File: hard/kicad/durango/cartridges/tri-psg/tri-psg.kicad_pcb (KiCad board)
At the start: 2 copper layers, 99.7 x 63.5 mm, 54 parts, among them J1 Durango_ROM, J2 CARTRIDGE, J20 PHONES, U1 74HC138, U10 SN76489A, U11 74HC574, U2 74HC08, U20 SN76489A, U21 74HC574, U22 SN76489A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

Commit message: cleanup and final triPSG opt
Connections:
- U2 pad 1: /LRDY -> /A4
- U2 pad 11: /A1·4 -> /~{LOE}
- U2 pad 12: /A4 -> /LRDY
- U2 pad 13: /A1 -> /~{L_PSG}
- U2 pad 2: /~{L_PSG} -> /A1
- U2 pad 3: /~{LOE} -> /A1·4
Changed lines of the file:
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@@
 			(layers "*.Cu" "*.Mask")
 			(remove_unused_layers no)
-			(net 65 "/LRDY")
+			(net 11 "/A4")
 			(pintype "input")
 		)
@@
 			(layers "*.Cu" "*.Mask")
 			(remove_unused_layers no)
-			(net 86 "/~{L_PSG}")
+			(net 8 "/A1")
 			(pintype "input")
 		)
@@
 			(layers "*.Cu" "*.Mask")
 			(remove_unused_layers no)
-			(net 94 "/~{LOE}")
+			(net 87 "/A1·4")
 			(pintype "output")
 		)
@@
 			(layers "*.Cu" "*.Mask")
 			(remove_unused_layers no)
-			(net 87 "/A1·4")
+			(net 94 "/~{LOE}")
 			(pintype "output")
 		)
@@
 			(layers "*.Cu" "*.Mask")
 			(remove_unused_layers no)
-			(net 11 "/A4")
+			(net 65 "/LRDY")
 			(pintype "input")
 		)
@@
 			(layers "*.Cu" "*.Mask")
 			(remove_unused_layers no)
-			(net 8 "/A1")
+			(net 86 "/~{L_PSG}")
 			(pintype "input")
 		)
@@
 		(tags "Resistor Axial_DIN0207 series Axial Vertical pin pitch 2.54mm 0.25W = 1/4W length 6.3mm diameter 2.5mm")
 		(property "Reference" "R1"
-			(at 1.27 -2.37 360)
+			(at 1.27 -2.37 0)
 			(layer "F.SilkS")
 			(effects
@@
 		)
 		(property "Value" "6K8"
-			(at 1.27 2.37 360)
+			(at 1.27 2.37 0)
 			(layer "F.Fab")
 			(effects
@@
 		)
 		(fp_text user "${REFERENCE}"
-			(at 1.27 -2.37 360)
+			(at 1.27 -2.37 0)
 			(layer "F.Fab")
 			(effects
@@
 		(tags "Resistor Axial_DIN0207 series Axial Vertical pin pitch 2.54mm 0.25W = 1/4W length 6.3mm diameter 2.5mm")
 		(property "Reference" "R2"
-			(at 1.27 -2.37 360)
+			(at 1.27 -2.37 0)
 			(layer "F.SilkS")
 			(effects
@@
 		)
 		(property "Value" "3K3"
-			(at 1.27 2.37 360)
+			(at 1.27 2.37 0)
 			(layer "F.Fab")
 			(effects
@@
 		)
 		(fp_text user "${REFERENCE}"
-			(at 1.27 -2.37 360)
+			(at 1.27 -2.37 0)
 			(layer "F.Fab")
 			(effects
@@
 		(tags "C Disc series Radial pin pitch 5.00mm  diameter 6mm width 2.5mm Capacitor")
 		(property "Reference" "C2"
-			(at 2.5 -2.5 360)
+			(at 2.5 -2.5 0)
 			(layer "F.SilkS")
 			(effects
@@
 		)
 		(property "Value" "22n"
-			(at 2.5 2.5 360)
+			(at 2.5 2.5 0)
 			(layer "F.Fab")
 			(effects
@@
 		)
 		(fp_text user "${REFERENCE}"
-			(at 2.5 0 360)
+			(at 2.5 0 0)
 			(layer "F.Fab")
 			(effects
@@
 		(tags "CP Radial series Radial pin pitch 2.50mm  diameter 6.3mm Electrolytic Capacitor")
 		(property "Reference" "C3"
-			(at 1.25 -4.4 360)
+			(at 1.25 -4.4 0)
 			(layer "F.SilkS")
 			(effects
@@
 		)
 		(property "Value" "470µ"
-			(at 1.25 4.4 360)
+			(at 1.25 4.4 0)
 			(layer "F.Fab")
 			(effects
@@
 		)
 		(fp_text user "${REFERENCE}"
-			(at 1.25 0 360)
+			(at 1.25 0 0)
 			(layer "F.Fab")
 			(effects

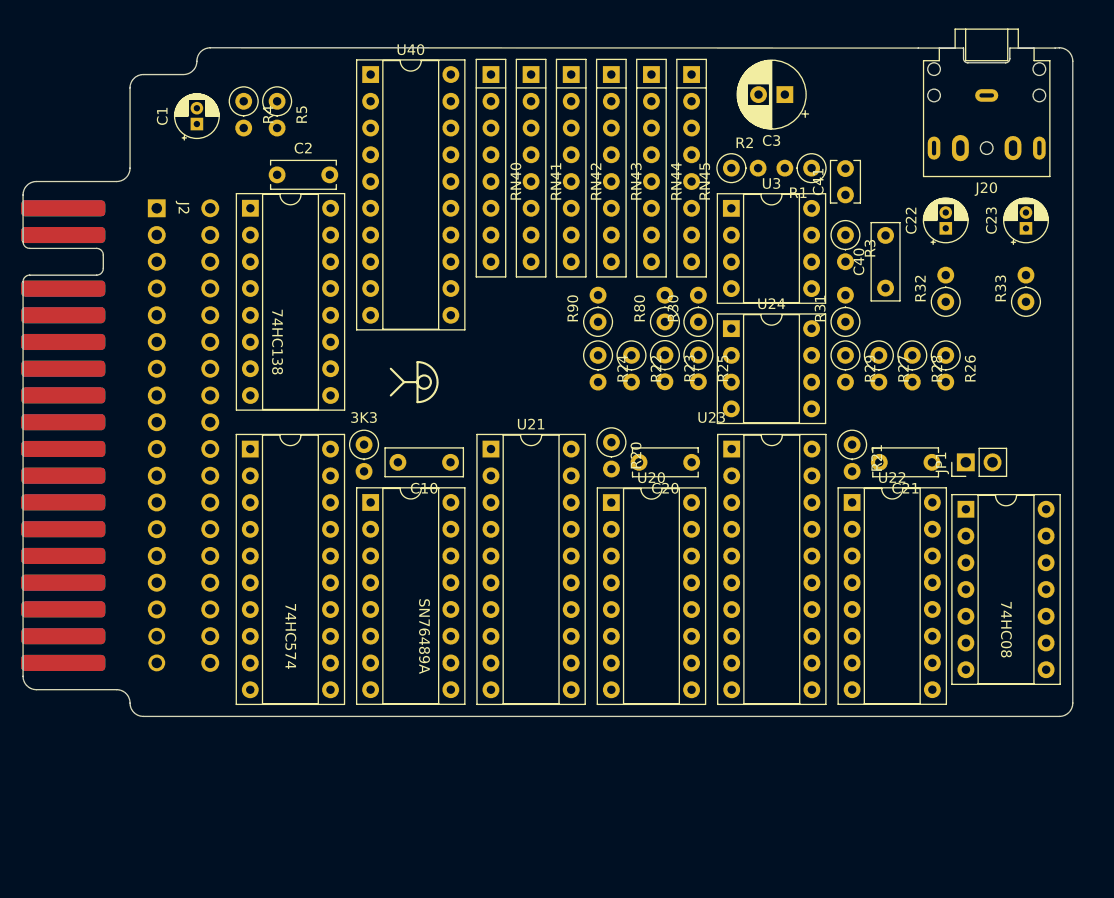
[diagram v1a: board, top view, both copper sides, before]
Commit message: 12 pads to enroute for triPSG
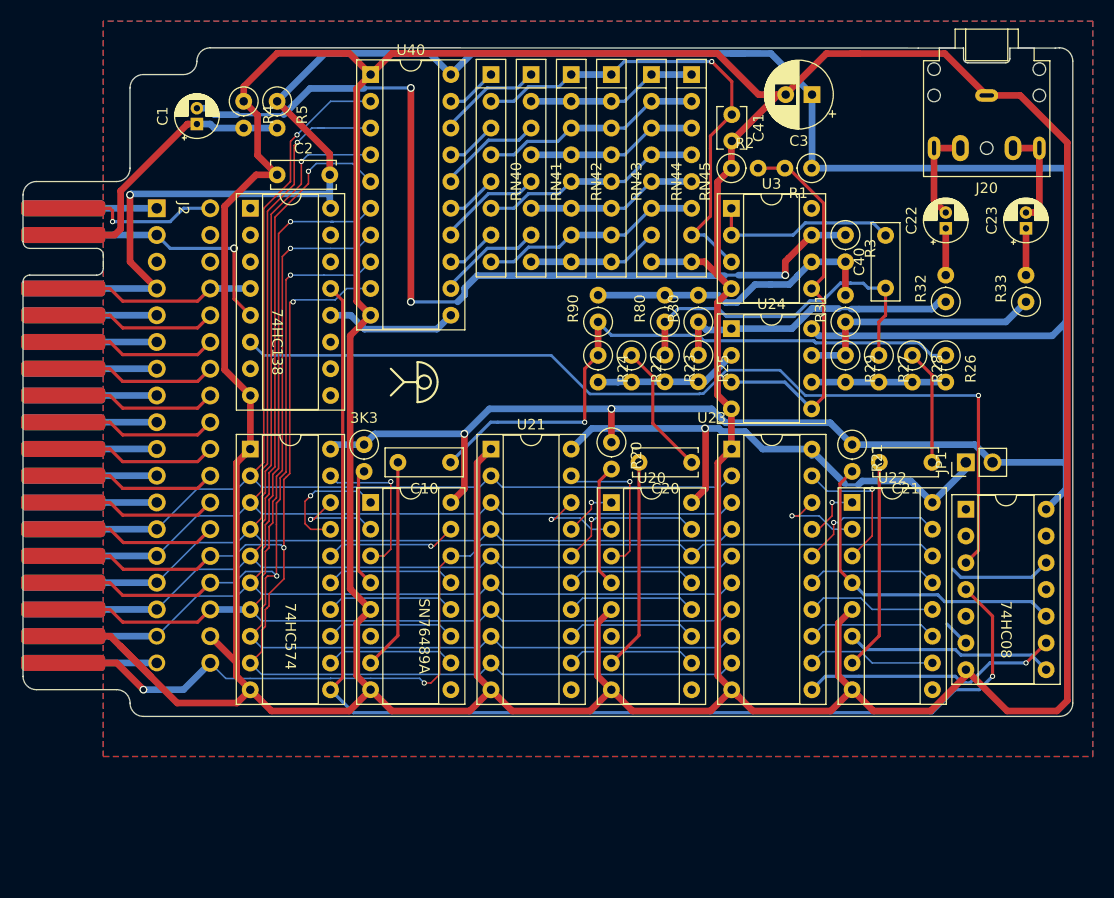
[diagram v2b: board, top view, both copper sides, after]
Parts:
- moved C41 13.2 mm to (92.7, 97.8), turned to -90 degrees
- moved C3 2.58 mm to (100.3, 95.9)
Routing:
- net GND: track 0.00 -> 499.8 mm
- net +5V: track 0.00 -> 280.4 mm, vias 0 -> 3
- net /D0: track 0.00 -> 114.1 mm, vias 0 -> 2
- net /D1: track 0.00 -> 114.0 mm, vias 0 -> 2
- net /~{PSG}: track 0.00 -> 113.6 mm, vias 0 -> 1
- net /D4: track 0.00 -> 113.1 mm, vias 0 -> 1
- net /D3: track 0.00 -> 111.9 mm, vias 0 -> 1
- net /D6: track 0.00 -> 111.5 mm, vias 0 -> 1
- net /D5: track 0.00 -> 111.2 mm, vias 0 -> 1
- net /D2: track 0.00 -> 110.3 mm, vias 0 -> 1
- net /D7: track 0.00 -> 109.9 mm, vias 0 -> 1
- net /VCLK: track 0.00 -> 98.2 mm, vias 0 -> 2
- net /A1·4: track 0.00 -> 89.5 mm, vias 0 -> 1
- net /MIX: track 0.00 -> 87.0 mm, vias 0 -> 3
- net /M_OUT: track 0.00 -> 58.7 mm, vias 0 -> 1
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- added copper zone on B.Cu, net +5V
- added copper zone on F.Cu, net GND

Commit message: fully enrouted triPSG
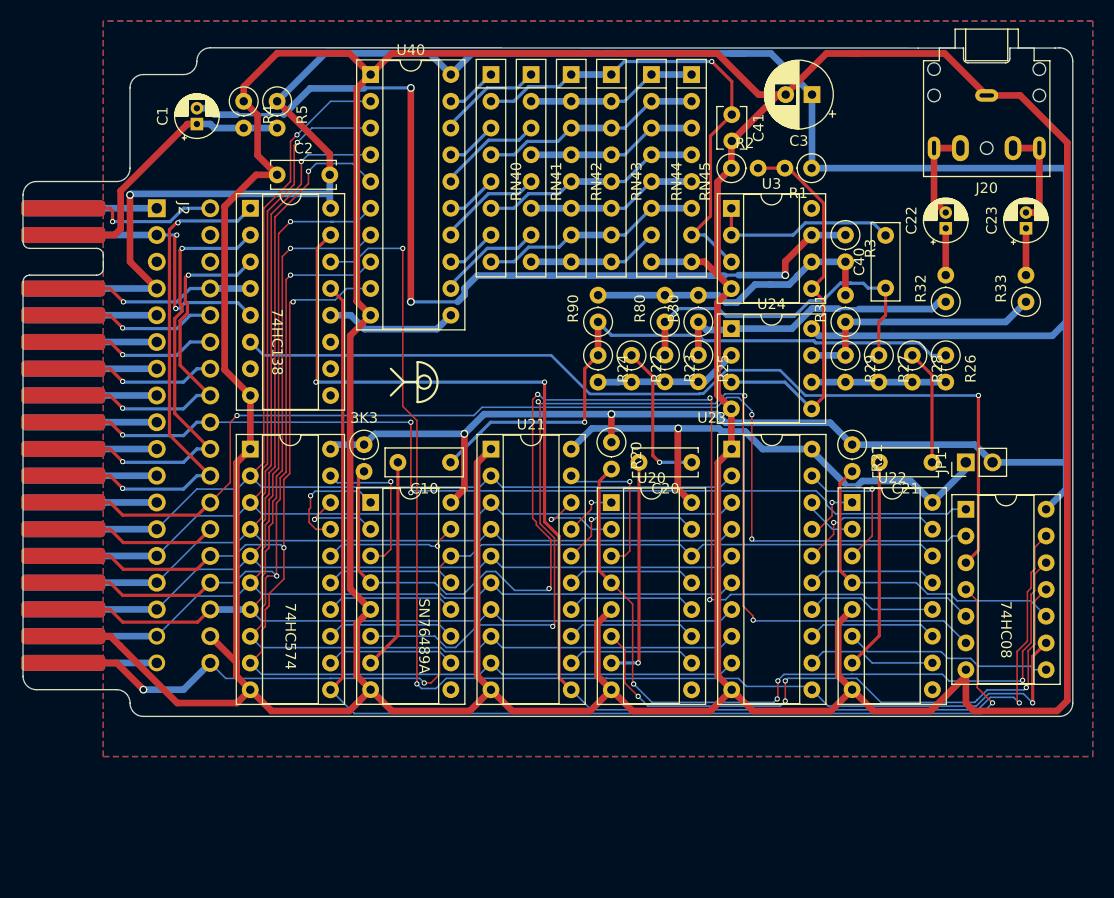
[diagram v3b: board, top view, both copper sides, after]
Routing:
- net /~{L_PSG}: track 0.00 -> 127.7 mm, vias 0 -> 3
- net /~{MOE}: track 2.54 -> 103.8 mm, vias 0 -> 4
- net /MRDY: track 11.3 -> 111.3 mm, vias 0 -> 4
- net /A1: track 15.0 -> 107.2 mm, vias 0 -> 3
- net /~{R_PSG}: track 24.6 -> 116.5 mm, vias 1 -> 3
- net /A4: track 15.0 -> 94.8 mm, vias 0 -> 3
- net /~{LOE}: track 0.00 -> 57.8 mm, vias 0 -> 4
- net /LRDY: track 21.5 -> 74.4 mm, vias 0 -> 4
- net /A2: track 15.0 -> 48.5 mm, vias 0 -> 2
- net /A3: track 15.0 -> 42.9 mm, vias 0 -> 2
- net /A5: track 15.0 -> 34.6 mm, vias 0 -> 2
- net /BR6: track 8.66 -> 5.20 mm, vias 1 -> 0
- net GND: track 499.8 -> 497.5 mm
- net /~{IOC}: track 23.7 -> 25.7 mm, vias 1 -> 2
- net /L_OUT: track 12.5 -> 14.3 mm, vias 0 -> 1
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
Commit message: improve ground planes on triPSG
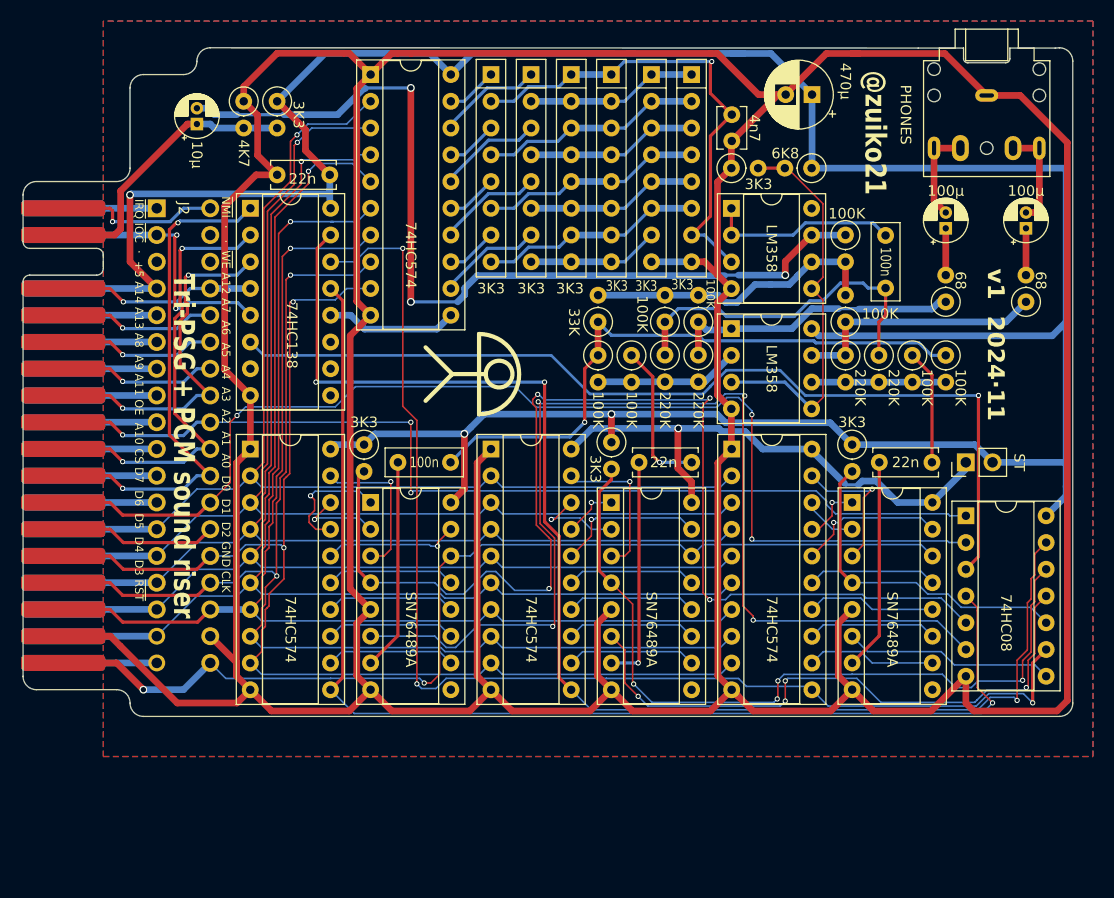
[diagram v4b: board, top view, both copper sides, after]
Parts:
- moved LOGO1 51.5 mm to (68.6, 123.2)
- moved U2 0.62 mm to (114.9, 135.9)
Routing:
- net /A1: track 107.2 -> 108.7 mm
- net /~{L_PSG}: track 127.7 -> 126.4 mm
- net GND: track 497.5 -> 496.3 mm
- net /MRDY: track 111.3 -> 111.9 mm
- net /~{R_PSG}: track 116.5 -> 115.9 mm
- net /~{PSG}: track 115.1 -> 114.5 mm
- net /A1·4: track 89.5 -> 90.1 mm
- net +5V: track 279.5 -> 280.1 mm
- net /~{LOE}: track 57.8 -> 57.2 mm
- net /D1: track 114.3 -> 113.8 mm
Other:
- board text added: "@zuiko21"
- board text added: "Tri-PSG + PCM sound riser"
- board text added: "v1 2024·11"
- board text added: "~{IRQ} ~{IOC} · +5 A14 A13 A8 A9 A11 OE A10 CS D7 D6 D5 D4 D3 ~{RST}"
- board text added: "~{NMI} · · ~{WE} A12 A7 A6 A5 A4 A3 A2 A1 A0 D0 D1 D2 GND CLK"

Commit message: fix silcreen on triPSG, ready for order
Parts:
- moved LOGO1 44.6 mm to (106.4, 99.6)
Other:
- board text added: "JLCJLCJLCJLC"
- board text added: "~{IRQ} ~{IOC} · +5 A14 A13 A8 A9 A11 ~{OE} A10 ~{CS} D7 D6 D5 D4 D3 ~{RST}"
- board text removed: "~{IRQ} ~{IOC} · +5 A14 A13 A8 A9 A11 OE A10 CS D7 D6 D5 D4 D3 ~{RST}"
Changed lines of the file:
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@@
 			(drillshape 0)
 			(scaleselection 1)
-			(outputdirectory "")
+			(outputdirectory "gerber/")
 		)
 	)
@@
 		)
 		(property "Value" "100n"
-			(at 2.5 0 270)
+			(at 2.5 0 -90)
 			(unlocked yes)
 			(layer "F.SilkS")
@@
 		)
 		(property "Value" "100K"
-			(at 2.667 1.143 270)
+			(at 2.667 1.143 -90)
 			(unlocked yes)
 			(layer "F.SilkS")
@@
 	(footprint "durango:j300"
 		(layer "B.Cu")
-		(at 68.58 123.19 90)
+		(at 106.426 99.568 90)
 		(property "Reference" "LOGO1"
 			(at 0 0 90)
@@
 		(layer "Edge.Cuts")
 	)
-	(gr_text "~{IRQ} ~{IOC}  ·  +5 A14 A13 A8  A9 A11 OE  A10 CS D7  D6  D5  D4  D3 ~{RST}"
+	(gr_text "JLCJLCJLCJLC"
+		(at 50.927 146.304 -90)
+		(layer "B.SilkS")
+		(effects
+			(font
+				(size 1 1)
+				(thickness 0.15)
+			)
+			(justify left bottom mirror)
+		)
+	)
+	(gr_text "~{IRQ} ~{IOC}  ·  +5 A14 A13 A8  A9 A11 ~{OE}  A10 ~{CS} D7  D6  D5  D4  D3 ~{RST}"
 		(at 35.941 105.791 270)
 		(layer "F.SilkS")
@@
 	)
 	(gr_text "v1  2024·11"
-		(at 116.84 112.395 270)
+		(at 122.047 117.983 270)
 		(layer "F.SilkS")
 		(effects
